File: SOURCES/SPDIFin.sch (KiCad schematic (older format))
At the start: 18 parts, among them P18 TST, U5 CS8422-CNZ

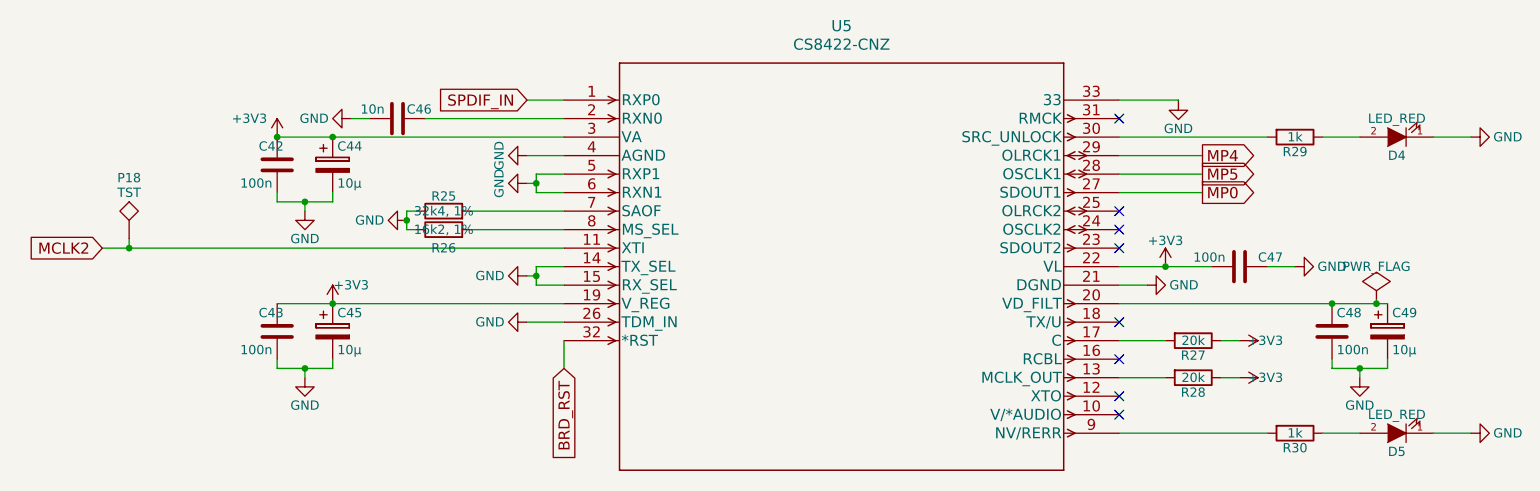
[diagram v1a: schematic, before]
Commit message: fixed SPDiF (RCA)
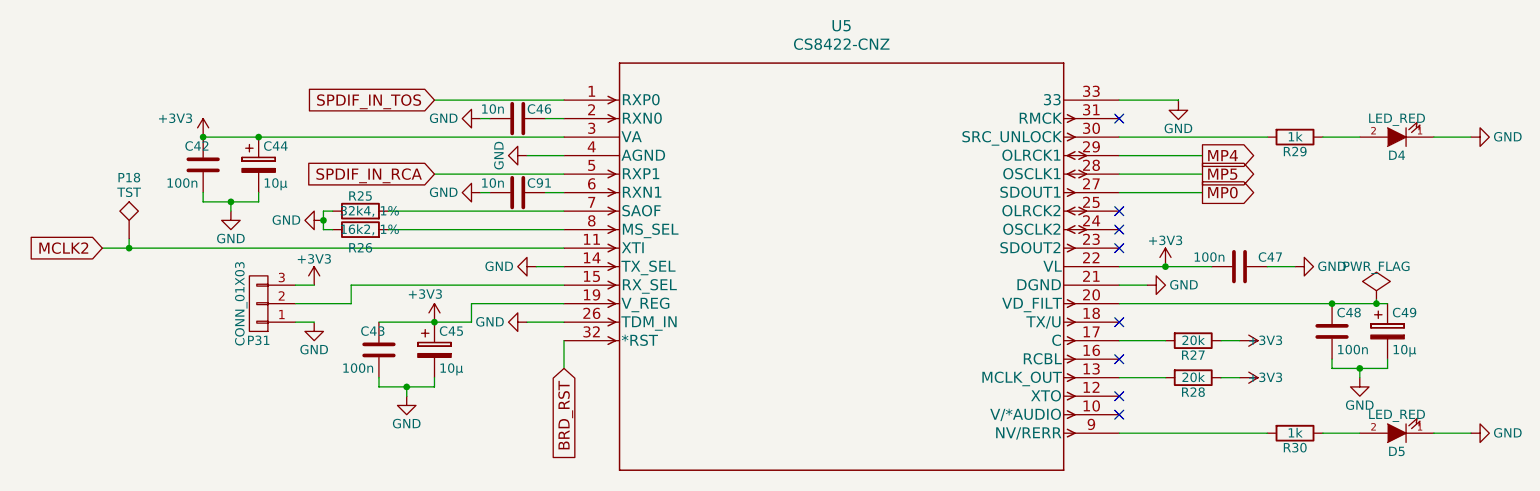
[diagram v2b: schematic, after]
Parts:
- added C91: 10n, fdsp_capacitor:C_1206_HandSoldering, symbol C
- added P31: CONN_01X03, symbol CONN_01X03
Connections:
- net +3V3: now also P31.3 (P3)
- net GND: now also C91.2, P31.1 (P1); no longer U5.15 (RX_SEL), U5.5 (RXP1), U5.6 (RXN1)
- net SPDIF_IN renamed SPDIF_IN_TOS
- new net: P31.2 (P2), U5.15 (RX_SEL)
- new net: C91.1, U5.6 (RXN1)
- new net SPDIF_IN_RCA: U5.5 (RXP1)
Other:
- moved on the sheet: C42, C43, C44, C45, C46, R25, R26

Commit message: layout incl. spdif
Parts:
- P31: footprint (none) -> fdsp_pinheader:Pin_Header_Straight_1x03
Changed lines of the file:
@@
 SPDIF_IN_TOS
 $Comp
-L GND #PWR76
+L GND #PWR068
 U 1 1 5B0AAA5E
 P 4150 4050
-F 0 "#PWR76" H 4150 3800 50  0001 C CNN
+F 0 "#PWR068" H 4150 3800 50  0001 C CNN
 F 1 "GND" V 4150 3850 50  0000 C CNN
 F 2 "" H 4150 4050 60  0000 C CNN
@@
 $EndComp
 $Comp
-L GND #PWR72
+L GND #PWR069
 U 1 1 5B0ABCD3
 P 3850 3250
-F 0 "#PWR72" H 3850 3000 50  0001 C CNN
+F 0 "#PWR069" H 3850 3000 50  0001 C CNN
 F 1 "GND" V 3850 3050 50  0000 C CNN
 F 2 "" H 3850 3250 60  0000 C CNN
@@
 $EndComp
 $Comp
-L GND #PWR74
+L GND #PWR070
 U 1 1 5B0AC2AB
 P 4100 3450
-F 0 "#PWR74" H 4100 3200 50  0001 C CNN
+F 0 "#PWR070" H 4100 3200 50  0001 C CNN
 F 1 "GND" H 4100 3300 50  0000 C CNN
 F 2 "" H 4100 3450 60  0000 C CNN
@@
 NoConn ~ 7300 3750
 $Comp
-L GND #PWR75
+L GND #PWR071
 U 1 1 5B0AC367
 P 4100 4350
-F 0 "#PWR75" H 4100 4100 50  0001 C CNN
+F 0 "#PWR071" H 4100 4100 50  0001 C CNN
 F 1 "GND" V 4100 4150 50  0000 C CNN
 F 2 "" H 4100 4350 60  0000 C CNN
@@
 $EndComp
 $Comp
-L GND #PWR70
+L GND #PWR072
 U 1 1 5B0AC5D5
 P 3450 4750
-F 0 "#PWR70" H 3450 4500 50  0001 C CNN
+F 0 "#PWR072" H 3450 4500 50  0001 C CNN
 F 1 "GND" H 3450 4600 50  0000 C CNN
 F 2 "" H 3450 4750 60  0000 C CNN
@@
 $EndComp
 $Comp
-L GND #PWR83
+L GND #PWR073
 U 1 1 5B0AC75C
 P 8600 4650
-F 0 "#PWR83" H 8600 4400 50  0001 C CNN
+F 0 "#PWR073" H 8600 4400 50  0001 C CNN
 F 1 "GND" H 8600 4500 50  0000 C CNN
 F 2 "" H 8600 4650 60  0000 C CNN
@@
 $EndComp
 $Comp
-L +3V3 #PWR71
+L +3V3 #PWR074
 U 1 1 5B0AC84E
 P 3600 4350
-F 0 "#PWR71" H 3600 4200 50  0001 C CNN
+F 0 "#PWR074" H 3600 4200 50  0001 C CNN
 F 1 "+3V3" H 3550 4500 50  0000 C CNN
 F 2 "" H 3600 4350 60  0000 C CNN
@@
 $EndComp
 $Comp
-L GND #PWR84
+L GND #PWR075
 U 1 1 5B0AD2EA
 P 9200 3350
-F 0 "#PWR84" H 9200 3100 50  0001 C CNN
+F 0 "#PWR075" H 9200 3100 50  0001 C CNN
 F 1 "GND" V 9200 3150 50  0000 C CNN
 F 2 "" H 9200 3350 60  0000 C CNN
@@
 $EndComp
 $Comp
-L GND #PWR77
+L GND #PWR076
 U 1 1 5B0AD75F
 P 7450 4150
-F 0 "#PWR77" H 7450 3900 50  0001 C CNN
+F 0 "#PWR076" H 7450 3900 50  0001 C CNN
 F 1 "GND" V 7450 3950 50  0000 C CNN
 F 2 "" H 7450 4150 60  0000 C CNN
@@
 $EndComp
 $Comp
-L GND #PWR82
+L GND #PWR077
 U 1 1 5B0AD8E4
 P 8250 4050
-F 0 "#PWR82" H 8250 3800 50  0001 C CNN
+F 0 "#PWR077" H 8250 3800 50  0001 C CNN
 F 1 "GND" V 8250 3850 50  0000 C CNN
 F 2 "" H 8250 4050 60  0000 C CNN
@@
 $EndComp
 $Comp
-L +3V3 #PWR80
+L +3V3 #PWR078
 U 1 1 5B0ADA22
 P 7950 4450
-F 0 "#PWR80" H 7950 4300 50  0001 C CNN
+F 0 "#PWR078" H 7950 4300 50  0001 C CNN
 F 1 "+3V3" V 7950 4590 50  0000 C CNN
 F 2 "" H 7950 4450 60  0000 C CNN
@@
 $EndComp
 $Comp
-L GND #PWR66
+L GND #PWR079
 U 1 1 5B0ADBC5
 P 2500 3750
-F 0 "#PWR66" H 2500 3500 50  0001 C CNN
+F 0 "#PWR079" H 2500 3500 50  0001 C CNN
 F 1 "GND" H 2500 3600 50  0000 C CNN
 F 2 "" H 2500 3750 60  0000 C CNN
@@
 $EndComp
 $Comp
-L +3V3 #PWR65
+L +3V3 #PWR080
 U 1 1 5B0ADBD2
 P 2350 3350
-F 0 "#PWR65" H 2350 3200 50  0001 C CNN
+F 0 "#PWR080" H 2350 3200 50  0001 C CNN
 F 1 "+3V3" H 2200 3450 50  0000 C CNN
 F 2 "" H 2350 3350 60  0000 C CNN
@@
 $EndComp
 $Comp
-L GND #PWR69
+L GND #PWR081
 U 1 1 5B0AE249
 P 3000 3800
-F 0 "#PWR69" H 3000 3550 50  0001 C CNN
+F 0 "#PWR081" H 3000 3550 50  0001 C CNN
 F 1 "GND" V 3000 3600 50  0000 C CNN
 F 2 "" H 3000 3800 60  0000 C CNN
@@
 $EndComp
 $Comp
-L +3V3 #PWR81
+L +3V3 #PWR082
 U 1 1 5B0AE79F
 P 7950 4650
-F 0 "#PWR81" H 7950 4500 50  0001 C CNN
+F 0 "#PWR082" H 7950 4500 50  0001 C CNN
 F 1 "+3V3" V 7950 4790 50  0000 C CNN
 F 2 "" H 7950 4650 60  0000 C CNN
@@
 $EndComp
 $Comp
-L GND #PWR85
+L GND #PWR083
 U 1 1 5B178F7C
 P 9200 4950
-F 0 "#PWR85" H 9200 4700 50  0001 C CNN
+F 0 "#PWR083" H 9200 4700 50  0001 C CNN
 F 1 "GND" V 9200 4750 50  0000 C CNN
 F 2 "" H 9200 4950 60  0000 C CNN
@@
 $EndComp
 $Comp
-L PWR_FLAG #FLG4
+L PWR_FLAG #FLG084
 U 1 1 5B19051F
 P 8690 4230
-F 0 "#FLG4" H 8690 4325 50  0001 C CNN
+F 0 "#FLG084" H 8690 4325 50  0001 C CNN
 F 1 "PWR_FLAG" H 8690 4410 50  0000 C CNN
 F 2 "" H 8690 4230 50  0000 C CNN
@@
 $EndComp
 $Comp
-L GND #PWR79
+L GND #PWR085
 U 1 1 5B1F0908
 P 7620 3155
-F 0 "#PWR79" H 7620 2905 50  0001 C CNN
+F 0 "#PWR085" H 7620 2905 50  0001 C CNN
 F 1 "GND" H 7620 3005 50  0000 C CNN
 F 2 "" H 7620 3155 60  0000 C CNN
@@
 Connection ~ 1950 3950
 $Comp
-L +3V3 #PWR78
+L +3V3 #PWR086
 U 1 1 5B22C9D1
 P 7550 4050
-F 0 "#PWR78" H 7550 3900 50  0001 C CNN
+F 0 "#PWR086" H 7550 3900 50  0001 C CNN
 F 1 "+3V3" H 7550 4190 50  0000 C CNN
 F 2 "" H 7550 4050 60  0000 C CNN
@@
 Connection ~ 7550 4050
 $Comp
-L GND #PWR68
+L GND #PWR087
 U 1 1 5B35E087
 P 2950 4350
-F 0 "#PWR68" H 2950 4100 50  0001 C CNN
+F 0 "#PWR087" H 2950 4100 50  0001 C CNN
 F 1 "GND" H 2950 4200 50  0000 C CNN
 F 2 "" H 2950 4350 60  0000 C CNN
@@
 $EndComp
 $Comp
-L +3V3 #PWR67
+L +3V3 #PWR088
 U 1 1 5B35E0E7
 P 2950 4150
-F 0 "#PWR67" H 2950 4000 50  0001 C CNN
+F 0 "#PWR088" H 2950 4000 50  0001 C CNN
 F 1 "+3V3" H 2950 4290 50  0000 C CNN
 F 2 "" H 2950 4150 60  0000 C CNN
@@
 $EndComp
 $Comp
-L GND #PWR73
+L GND #PWR089
 U 1 1 5B35FA83
 P 3850 3650
-F 0 "#PWR73" H 3850 3400 50  0001 C CNN
+F 0 "#PWR089" H 3850 3400 50  0001 C CNN
 F 1 "GND" V 3850 3450 50  0000 C CNN
 F 2 "" H 3850 3650 60  0000 C CNN
@@
 F 0 "P31" H 2650 4450 50  0000 C CNN
 F 1 "CONN_01X03" V 2750 4250 50  0000 C CNN
-F 2 "" H 2650 4250 60  0000 C CNN
+F 2 "fdsp_pinheader:Pin_Header_Straight_1x03" H 2650 4250 60  0001 C CNN
 F 3 "" H 2650 4250 60  0000 C CNN
 	1    2650 4250

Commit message: updated references
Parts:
- C44, C45, C49: value 10µ -> 10u
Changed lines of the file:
@@
 P 3600 4500
 F 0 "C45" H 3625 4600 50  0000 L CNN
-F 1 "10µ" H 3625 4400 50  0000 L CNN
+F 1 "10u" H 3625 4400 50  0000 L CNN
 F 2 "fdsp_capacitor:C_Radial_D5_L11_P2" H 3638 4350 30  0001 C CNN
 F 3 "" H 3600 4500 60  0000 C CNN
@@
 P 8750 4400
 F 0 "C49" H 8775 4500 50  0000 L CNN
-F 1 "10µ" H 8775 4300 50  0000 L CNN
+F 1 "10u" H 8775 4300 50  0000 L CNN
 F 2 "fdsp_capacitor:C_Radial_D5_L11_P2" H 8788 4250 30  0001 C CNN
 F 3 "" H 8750 4400 60  0000 C CNN
@@
 P 2650 3500
 F 0 "C44" H 2675 3600 50  0000 L CNN
-F 1 "10µ" H 2675 3400 50  0000 L CNN
+F 1 "10u" H 2675 3400 50  0000 L CNN
 F 2 "fdsp_capacitor:C_Radial_D5_L11_P2" H 2688 3350 30  0001 C CNN
 F 3 "" H 2650 3500 60  0000 C CNN
